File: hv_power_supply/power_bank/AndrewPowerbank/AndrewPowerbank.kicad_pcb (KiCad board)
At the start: 2 copper layers, 48.3 x 30.5 mm, 47 parts, among them J1 NanoFit_RA_TH_02, J2 NanoFit_RA_TH_02, J3 USB-A-S-X-X-SM2, J4 USB-Micro-1981568-1, J5 NanoFit_RA_TH_02, Q1 SSM3K333R, U1 MCP73871T-2CCI_ML, U2 TPS61090RSAR

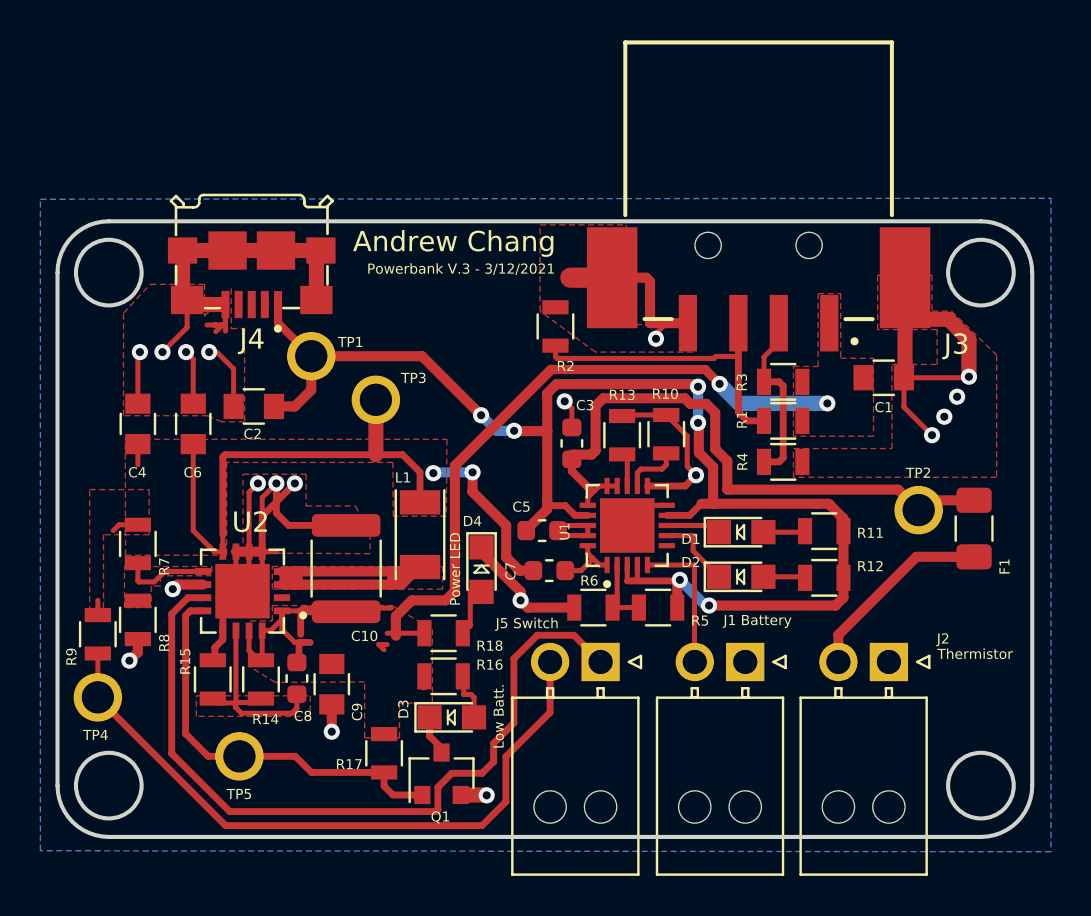
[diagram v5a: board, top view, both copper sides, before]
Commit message: Revise board so that J3 USB A input is better-fitted, components are more space-efficient.
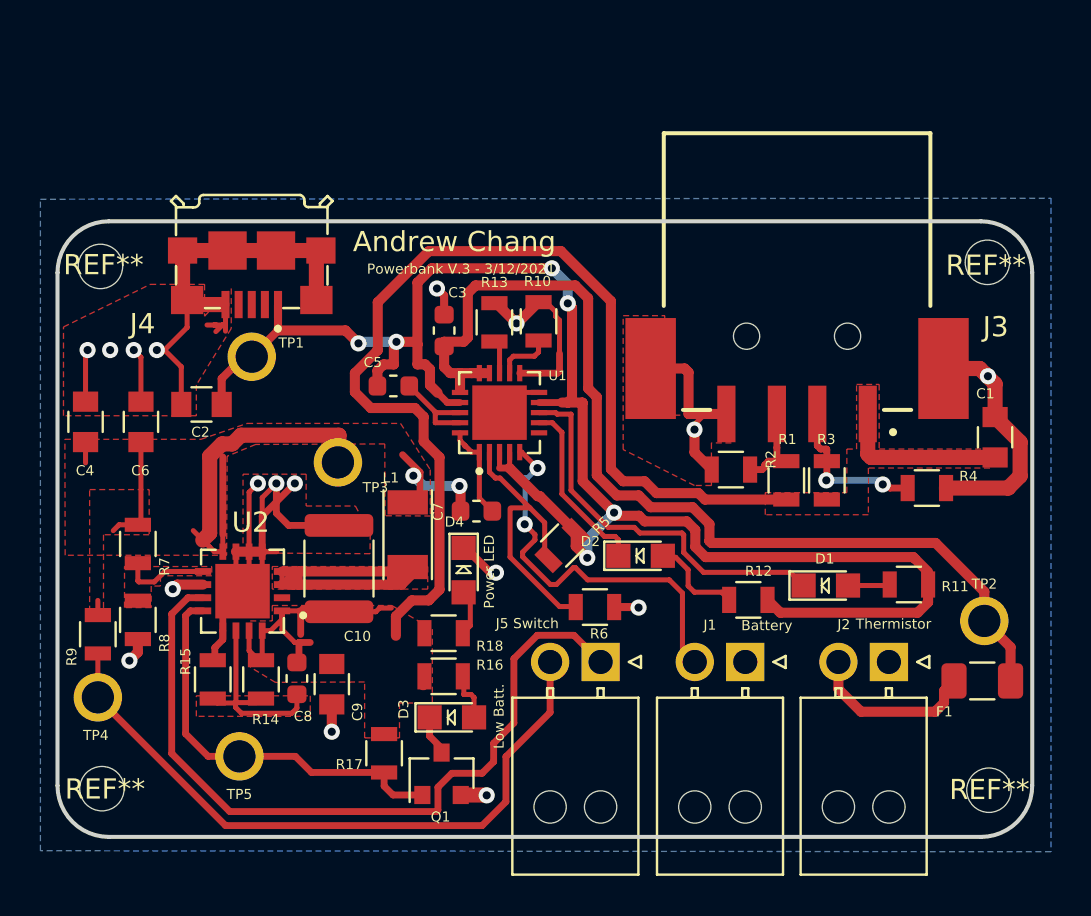
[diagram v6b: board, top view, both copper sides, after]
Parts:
- added REF**: MountingHole_2.2mm_M2, MountingHole:MountingHole_2.2mm_M2, F.Cu at (77.4, 73.8)
- added REF**: MountingHole_2.2mm_M2, MountingHole:MountingHole_2.2mm_M2, F.Cu at (33.5, 99.9)
- added REF**: MountingHole_2.2mm_M2, MountingHole:MountingHole_2.2mm_M2, F.Cu at (33.5, 74.0)
- added REF**: MountingHole_2.2mm_M2, MountingHole:MountingHole_2.2mm_M2, F.Cu at (77.4, 100.0)
- moved R2 11.2 mm to (64.7, 84.1), turned to 180 degrees
- moved C5 10.3 mm to (48.0, 80.0)
- moved C3 8.44 mm to (50.5, 77.2)
- moved R10 8.44 mm to (55.1, 76.8)
- moved R13 8.44 mm to (53.0, 76.8)
- moved U1 8.44 mm to (53.2, 81.3)
- moved F1 7.55 mm to (77.1, 94.6), turned to 0 degrees
- moved R4 7.23 mm to (74.4, 85.0)
- moved TP2 6.38 mm to (77.2, 91.6)
- moved C1 6.25 mm to (77.7, 82.5), turned to 90 degrees
- moved R5 5.66 mm to (56.3, 87.9), turned to 45 degrees
- moved R3 5.33 mm to (69.4, 84.6), turned to 270 degrees
- moved D2 5.09 mm to (60.2, 88.4)
- moved D1 4.95 mm to (69.4, 89.8)
- moved R11 4.95 mm to (73.5, 89.8)
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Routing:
- net +5V: track 51.9 -> 78.5 mm, vias 2 -> 0
- net /Battery+: track 31.1 -> 50.2 mm
- net Net-(D1-Pad1): track 2.58 -> 19.4 mm
- net /16KThermistor: track 7.47 -> 19.7 mm, vias 0 -> 2
- net Net-(J3-Pad03): track 15.5 -> 4.09 mm
- net VBUS: track 72.3 -> 83.7 mm
- net Net-(R5-Pad1): track 3.81 -> 14.3 mm
- net GND: track 108.8 -> 101.6 mm, vias 19 -> 17
- net Net-(D2-Pad1): track 3.88 -> 8.91 mm
- net Net-(D2-Pad2): track 2.09 -> 5.09 mm
- net +BATT: track 36.8 -> 33.9 mm
- net Net-(C7-Pad1): track 3.21 -> 4.81 mm
- net Net-(C5-Pad2): track 3.65 -> 4.81 mm
- net Net-(F1-Pad1): track 9.66 -> 8.51 mm
- net Net-(J3-Pad02): track 9.57 -> 9.52 mm, vias 0 -> 2
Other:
- outline, holes or cut-outs redrawn

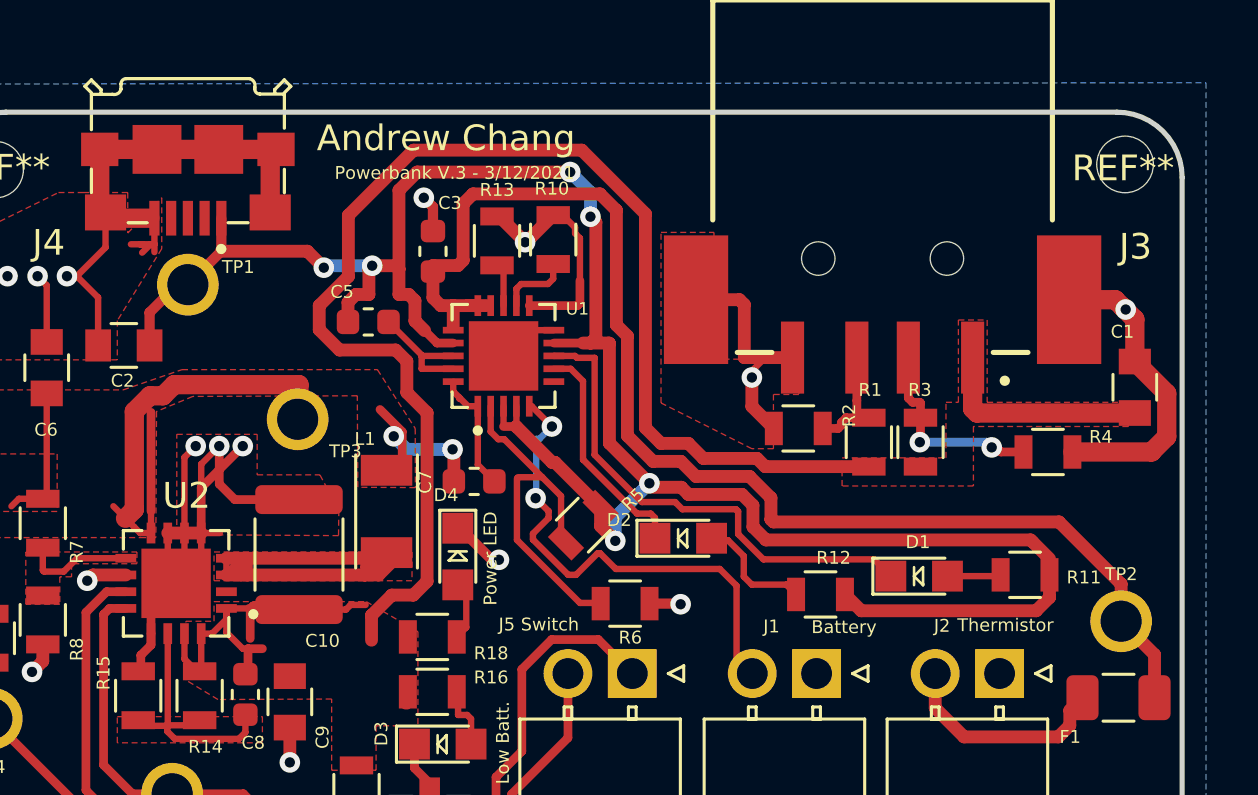
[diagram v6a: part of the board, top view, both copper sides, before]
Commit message: Make component labels clearer.
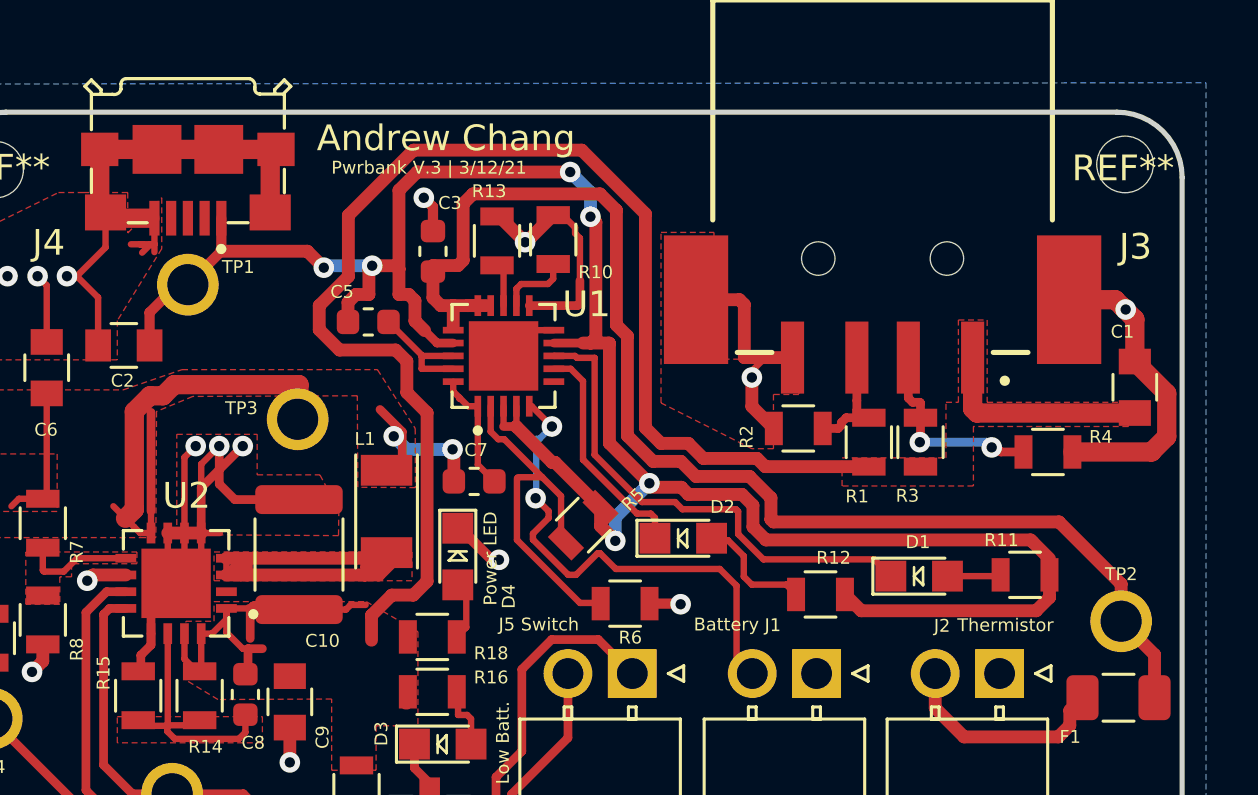
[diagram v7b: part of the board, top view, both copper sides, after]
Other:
- board text added: "Pwrbank V.3 | 3/12/21"
- board text removed: "Powerbank V.3 - 3/12/2021"
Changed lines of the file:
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@@
   (layers
     (0 F.Cu signal)
-    (31 B.Cu signal)
+    (31 B.Cu signal hide)
     (32 B.Adhes user)
     (33 F.Adhes user)
@@
     (tags "resistor 0805")
     (attr smd)
-    (fp_text reference R13 (at 1.9812 0 180) (layer F.SilkS)
+    (fp_text reference R13 (at 1.9304 -0.3048 180) (layer F.SilkS)
       (effects (font (size 0.5 0.5) (thickness 0.125)))
     )
@@
     (descr "Molex Nano Fit, single row, side entry, through hole, Datasheet:http://www.molex.com/pdm_docs/sd/1053131208_sd.pdf")
     (tags "connector molex nano-fit 105313-xx04")
-    (fp_text reference J1 (at 1.7526 1.8288) (layer F.SilkS)
+    (fp_text reference J1 (at 1.7018 1.8796) (layer F.SilkS)
       (effects (font (size 0.5 0.5) (thickness 0.12)))
     )
@@
     (tags capacitor)
     (attr smd)
-    (fp_text reference C7 (at 1.905 -0.0254 90) (layer F.SilkS)
+    (fp_text reference C7 (at -0.0762 1.2192 180) (layer F.SilkS)
       (effects (font (size 0.5 0.5) (thickness 0.125)))
     )
@@
     (tags "LED led 0805 SMD smd SMT smt smdled SMDLED smtled SMTLED")
     (attr smd)
-    (fp_text reference D2 (at -2.4892 -0.7112) (layer F.SilkS)
+    (fp_text reference D2 (at 1.524 -1.2192) (layer F.SilkS)
       (effects (font (size 0.5 0.5) (thickness 0.125)))
     )
@@
     (tags "LED led 0805 SMD smd SMT smt smdled SMDLED smtled SMTLED")
     (attr smd)
-    (fp_text reference D4 (at -2.3876 0.4572 180) (layer F.SilkS)
+    (fp_text reference D4 (at 1.5494 -1.9812 270) (layer F.SilkS)
       (effects (font (size 0.5 0.5) (thickness 0.125)))
     )
@@
     (tags "resistor 0805")
     (attr smd)
-    (fp_text reference R1 (at 2.032 0.0508) (layer F.SilkS)
+    (fp_text reference R1 (at -2.1082 -0.4572) (layer F.SilkS)
       (effects (font (size 0.5 0.5) (thickness 0.125)))
     )
@@
     (tags "resistor 0805")
     (attr smd)
-    (fp_text reference R2 (at -1.9812 0.508 270) (layer F.SilkS)
+    (fp_text reference R2 (at 2.0066 -0.3302 270) (layer F.SilkS)
       (effects (font (size 0.5 0.5) (thickness 0.125)))
     )
@@
     (tags "resistor 0805")
     (attr smd)
-    (fp_text reference R3 (at -2.032 0.0254) (layer F.SilkS)
+    (fp_text reference R3 (at 2.0828 0.508) (layer F.SilkS)
       (effects (font (size 0.5 0.5) (thickness 0.125)))
     )
@@
     (tags "resistor 0805")
     (attr smd)
-    (fp_text reference R10 (at 1.9812 -0.0508 180) (layer F.SilkS)
+    (fp_text reference R10 (at -1.27 1.651 180) (layer F.SilkS)
       (effects (font (size 0.5 0.5) (thickness 0.125)))
     )
@@
     (tags "resistor 0805")
     (attr smd)
-    (fp_text reference R11 (at -2.286 -0.1016) (layer F.SilkS)
+    (fp_text reference R11 (at 0.9144 1.3462) (layer F.SilkS)
       (effects (font (size 0.5 0.5) (thickness 0.125)))
     )
@@
   (module footprints:tp_1.6mm (layer F.Cu)
     (at 45.212 83.7438)
-    (fp_text reference TP3 (at 1.8542 1.2446) (layer F.SilkS)
+    (fp_text reference TP3 (at -2.1844 -0.4318) (layer F.SilkS)
       (effects (font (size 0.5 0.5) (thickness 0.125)))
     )
@@
   (module footprints:MCP73871T (layer F.Cu)
     (at 53.213 81.28 90)
-    (fp_text reference U1 (at 1.8288 2.8702 180) (layer F.SilkS)
-      (effects (font (size 0.48 0.48) (thickness 0.12)))
+    (fp_text reference U1 (at 2.0066 3.2258 180) (layer F.SilkS)
+      (effects (font (size 1 1) (thickness 0.2)))
     )
     (fp_text value MCP73871T-2CCI_ML (at -4.0132 7.2644 180) (layer F.Fab)
@@
     (at 40.4876 90.1192 180)
     (fp_text reference U2 (at -0.4064 3.4036) (layer F.SilkS)
-      (effects (font (size 1.00111 1.00111) (thickness 0.2)))
+      (effects (font (size 1 1) (thickness 0.2)))
     )
     (fp_text value TPS61090RSAR (at 2.032 -10.7696) (layer F.Fab)
@@
     (effects (font (size 0.5 0.5) (thickness 0.125)))
   )
-  (gr_text Battery (at 66.4464 91.821) (layer F.SilkS)
+  (gr_text Battery (at 61.8744 91.7194) (layer F.SilkS)
     (effects (font (size 0.5 0.5) (thickness 0.125)))
   )
@@
     (effects (font (size 0.5 0.5) (thickness 0.125)))
   )
-  (gr_text "Powerbank V.3 - 3/12/2021" (at 51.308 74.168) (layer F.SilkS)
+  (gr_text "Pwrbank V.3 | 3/12/21" (at 50.3174 73.9648) (layer F.SilkS)
     (effects (font (size 0.5 0.5) (thickness 0.125)))
   )

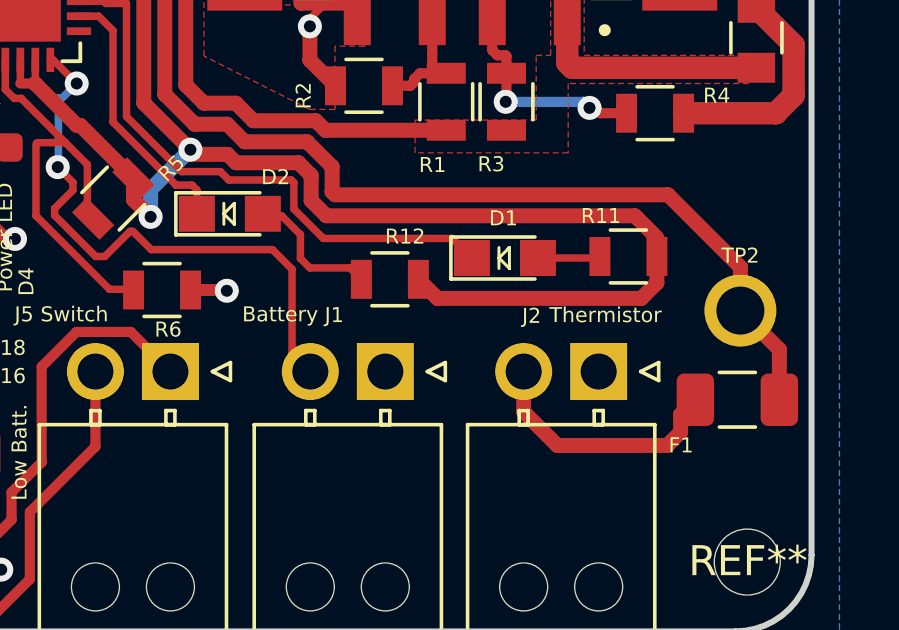
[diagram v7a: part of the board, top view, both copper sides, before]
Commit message: Fix switched Thermistor and Battery labels on connection ports.
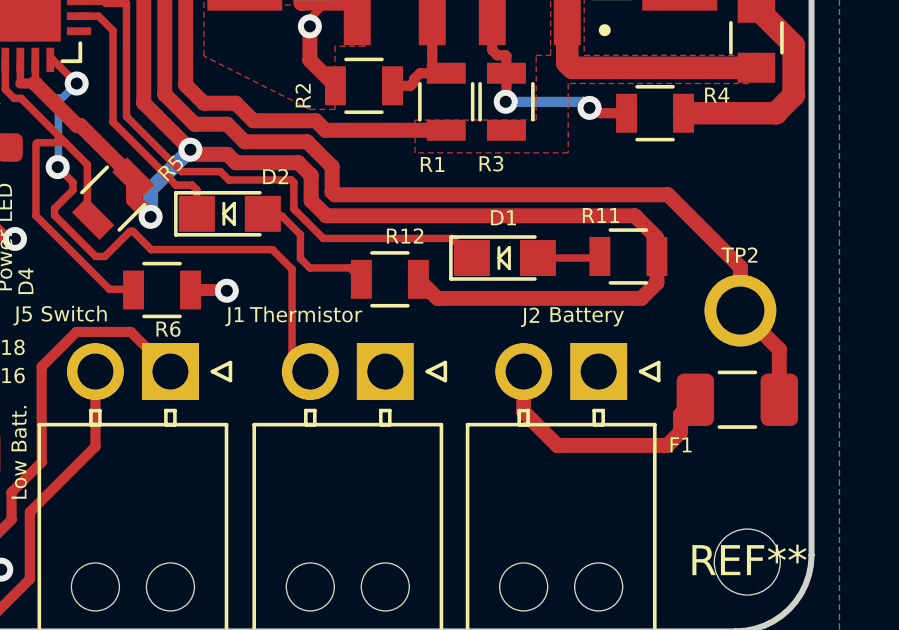
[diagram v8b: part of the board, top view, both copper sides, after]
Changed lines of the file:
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@@
     (descr "Molex Nano Fit, single row, side entry, through hole, Datasheet:http://www.molex.com/pdm_docs/sd/1053131208_sd.pdf")
     (tags "connector molex nano-fit 105313-xx04")
-    (fp_text reference J1 (at 1.7018 1.8796) (layer F.SilkS)
+    (fp_text reference J1 (at 4.9784 1.8796) (layer F.SilkS)
       (effects (font (size 0.5 0.5) (thickness 0.12)))
     )
@@
     (effects (font (size 0.5 0.5) (thickness 0.125)))
   )
-  (gr_text Battery (at 61.8744 91.7194) (layer F.SilkS)
+  (gr_text Battery (at 72.0852 91.7448) (layer F.SilkS)
     (effects (font (size 0.5 0.5) (thickness 0.125)))
   )
-  (gr_text Thermistor (at 72.7202 91.7448) (layer F.SilkS)
+  (gr_text Thermistor (at 62.738 91.7448) (layer F.SilkS)
     (effects (font (size 0.5 0.5) (thickness 0.125)))
   )
